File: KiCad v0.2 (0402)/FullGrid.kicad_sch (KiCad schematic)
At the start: 202 parts, among them J1 Conn_01x16

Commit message: Uhm
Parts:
- added D202, D203, D204, D205, D206, D207: WL-SMCC_0402, WL-SMCC_0402:WL-SMCC_0402, symbol WL-SMCC_0402:WL-SMCC_0402
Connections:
- new net: D202.1, D203.2, D206.1, D207.2
- new net: D204.2, D205.1, D206.2, D207.1
- new net: D202.2, D203.1, D204.1, D205.2
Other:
- note added: "+"
- note added: "-"
- note added: "Z"

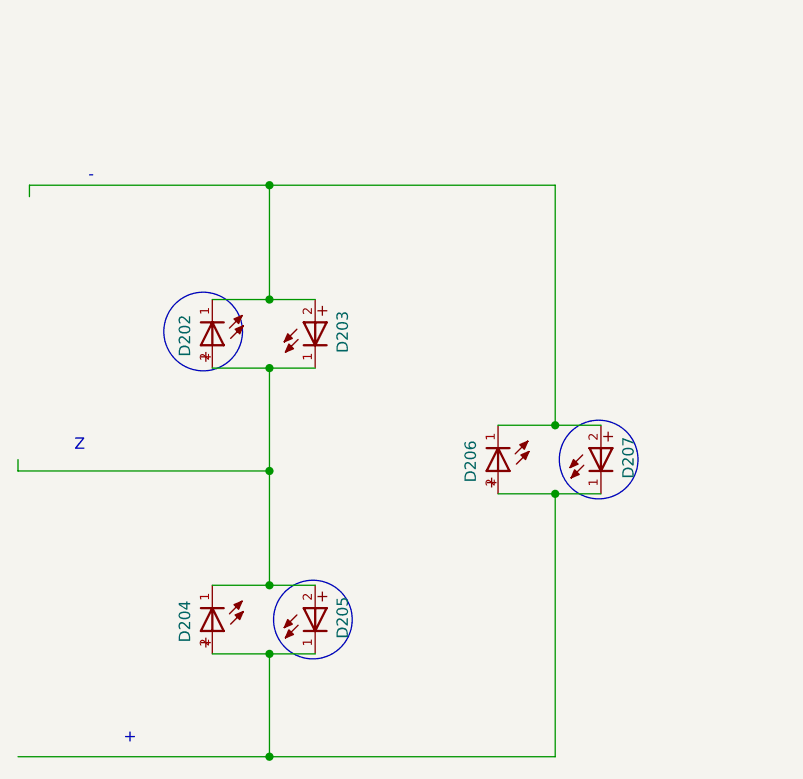
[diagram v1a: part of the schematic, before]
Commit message: v0.3 sent for fab, v0.4 still in progress
v0.3 and v0.4 have the same component footprints - that way, I only need to have 1 stencil (if v0.3 works!!!)
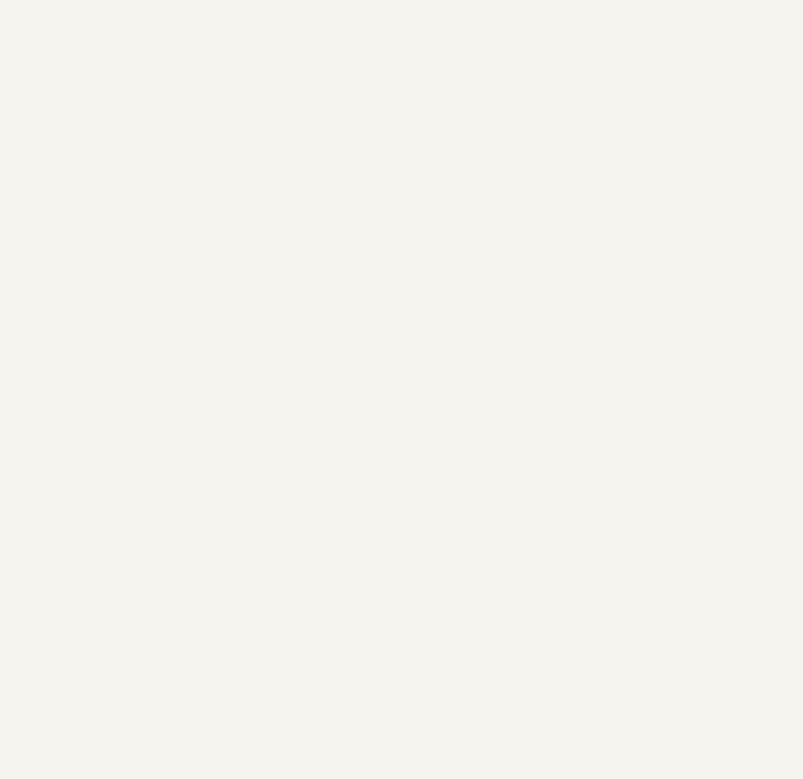
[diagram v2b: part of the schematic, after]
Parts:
- removed D202, D203, D204, D205, D206, D207: WL-SMCC_0402, WL-SMCC_0402:WL-SMCC_0402, symbol WL-SMCC_0402:WL-SMCC_0402
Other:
- note removed: "+"
- note removed: "-"
- note removed: "Z"
